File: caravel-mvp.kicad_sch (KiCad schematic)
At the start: 47 parts, among them J2 Conn_01x02, J3 Conn_02x04_Odd_Even, J4 Conn_01x06, J6 Conn_02x18_Odd_Even, J6 USB_C_Receptacle_USB2.0, J9 613012243121, SW3 B3U-1000P, U1 Caravel_QFN, U1 W25Q32JVSS, X1 10MHz

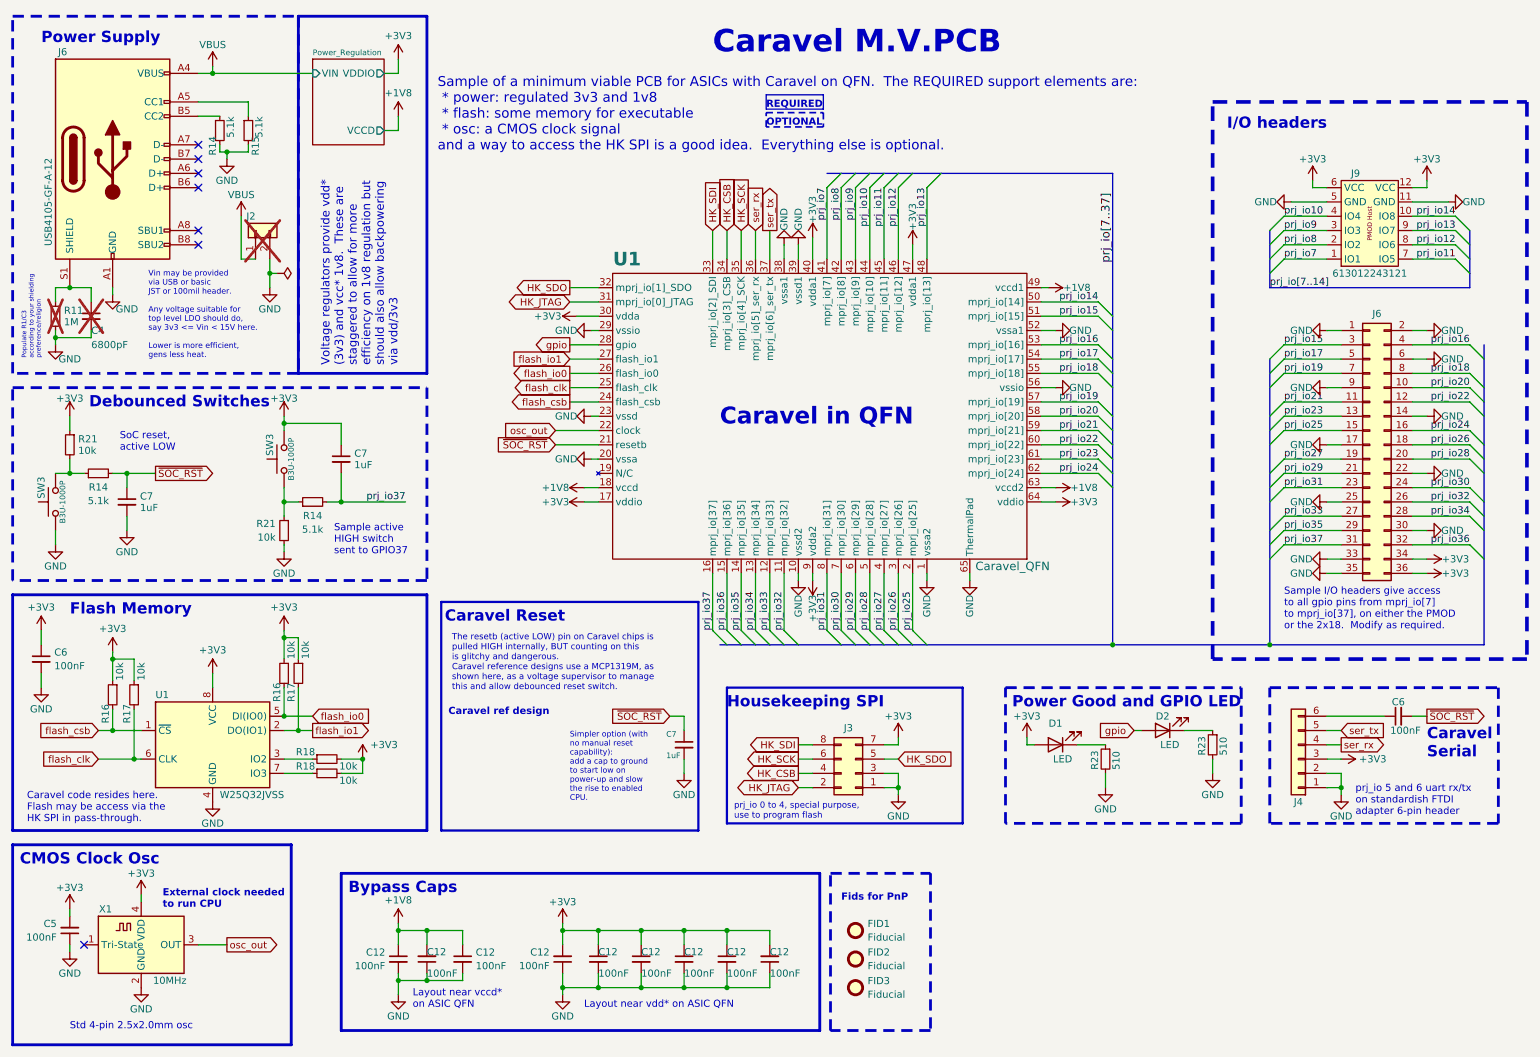
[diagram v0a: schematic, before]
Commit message: Comment clarifications
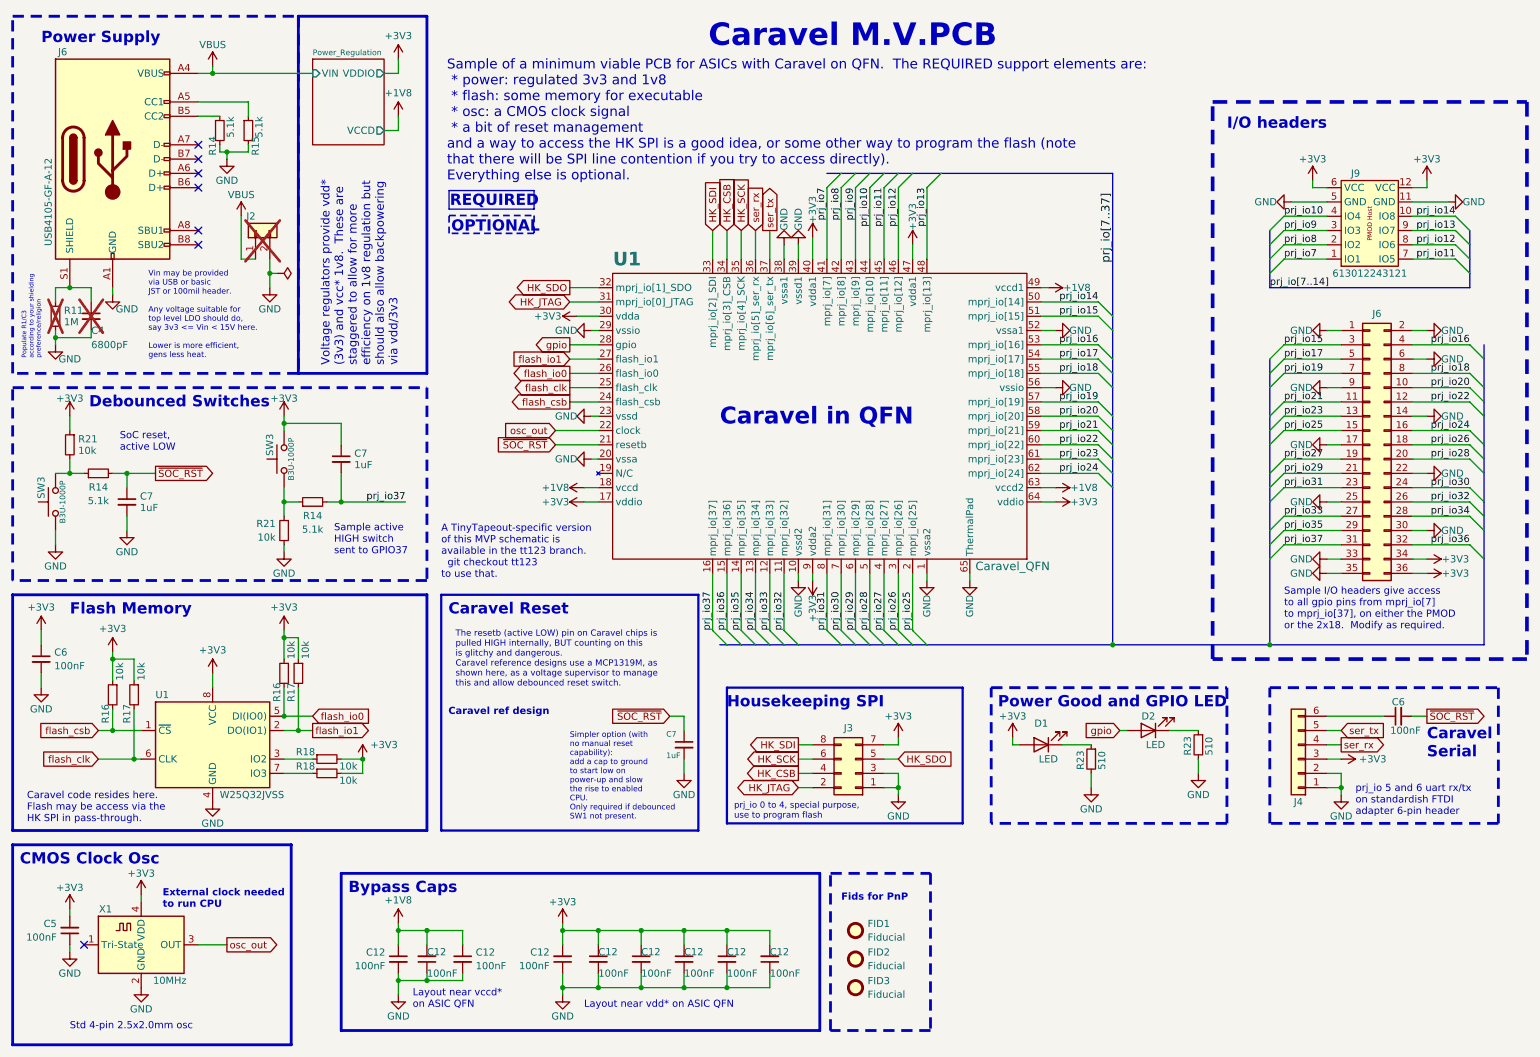
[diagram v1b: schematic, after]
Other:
- note added: "A TinyTapeout-specific version of this MVP schematic is available in the tt123 branch. git checkout tt123 to use that."
- note added: "Sample of a minimum viable PCB for ASICs with Caravel on QFN. The REQUIRED support elements are: * power: regulated 3v3 and 1v8 * flash: some memory for executable * osc: a CMOS clock signal * a bit of reset management and a way to access the HK SPI is a good idea, or some other way to program the flash (note that there will be SPI line contention if you try to access directly). Everything else i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"
- note added: "Simpler option (with no manual reset capability): add a cap to ground to start low on power-up and slow the rise to enabled CPU. Only required if debounced SW1 not present."
- note removed: "Sample of a minimum viable PCB for ASICs with Caravel on QFN. The REQUIRED support elements are: * power: regulated 3v3 and 1v8 * flash: some memory for executable * osc: a CMOS clock signal and a way to access the HK SPI is a good idea. Everything else is optional."
- note removed: "Simpler option (with no manual reset capability): add a cap to ground to start low on power-up and slow the rise to enabled CPU."
- moved on the sheet: D1, D2, R23

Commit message: Cleanups and even more clarifications in comments
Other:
- note added: "JTAG pin optional but the SPI is needed to access flash without contention from caravel."
- moved on the sheet: C12, FID1, FID2, FID3, J3
